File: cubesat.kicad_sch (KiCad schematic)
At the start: 7 parts, among them U1 MCP9808_MSOP, U2 MPU-6050

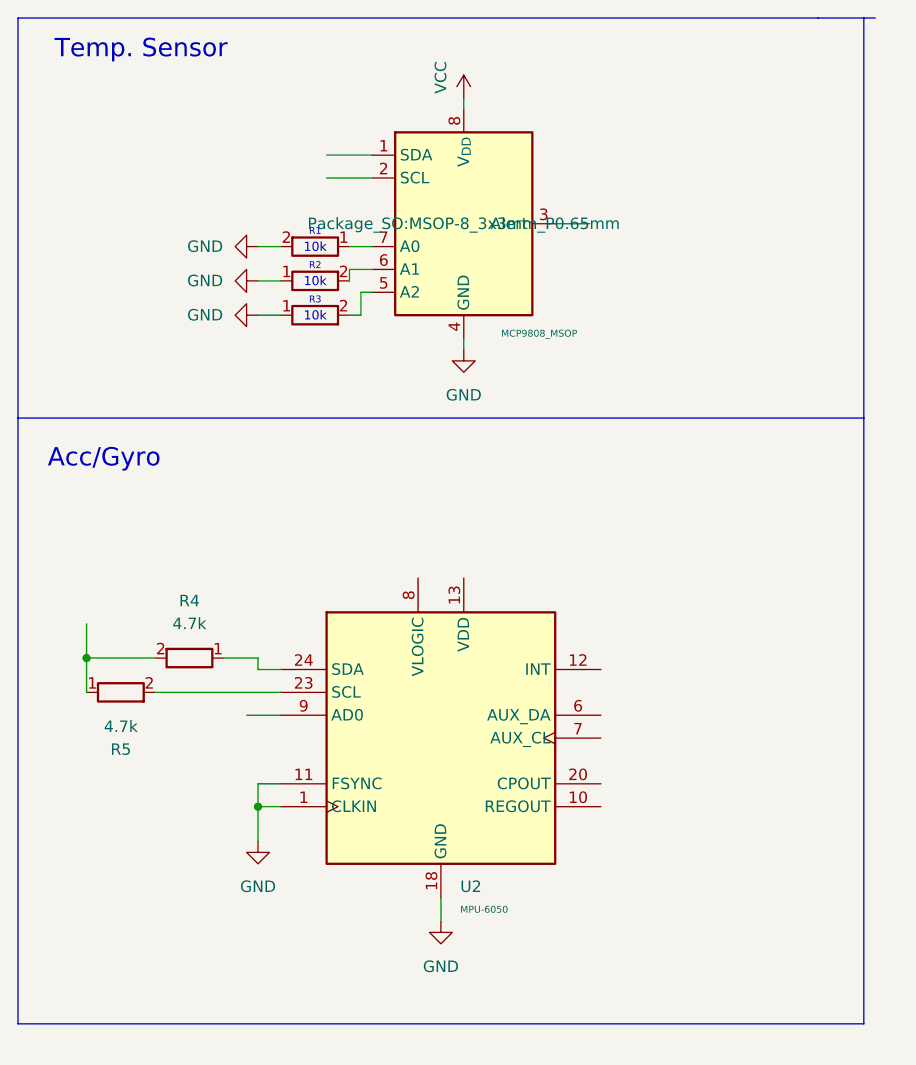
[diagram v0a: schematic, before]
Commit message: add mpu schéma
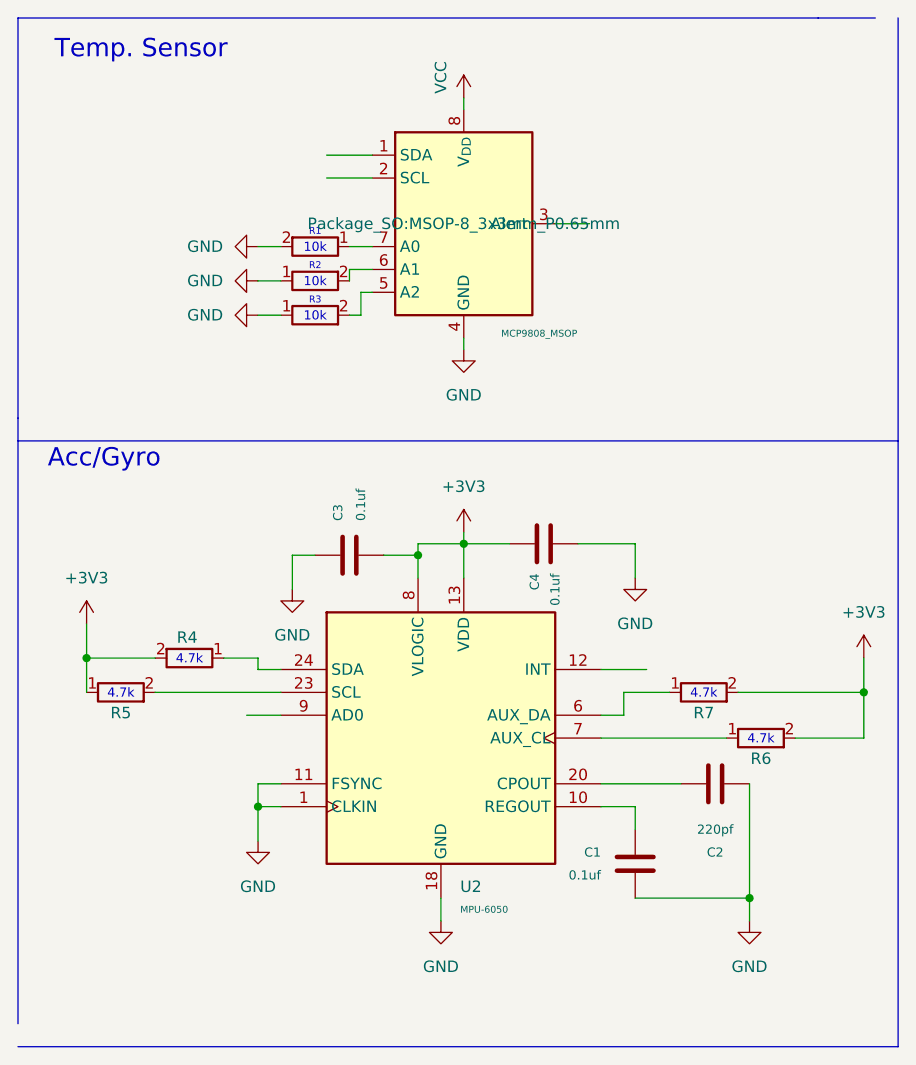
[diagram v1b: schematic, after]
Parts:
- added C1, C3, C4: 0.1uf, symbol Device:C
- added C2: 220pf, symbol Device:C
- added R6, R7: 4.7k, Resistor_SMD:R_0201_0603Metric, symbol Device:R
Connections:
- net GND: now also C1.2, C2.1, C3.1, C4.2
- net +3V3: now reaches R4.2, R5.1
- net +3V3: now also U2.13 (VDD), U2.8 (VLOGIC), C3.2, C4.1, R6.2, R7.2
- net at U2.10 (REGOUT): now also C1.1
- net at U2.20 (CPOUT): now also C2.2
- net at U2.6 (AUX_DA): now also R7.1
- net at U2.7 (AUX_CL): now also R6.1
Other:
- note added: "4.7k"
